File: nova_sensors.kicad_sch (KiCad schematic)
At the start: 91 parts, among them J1 Conn_01x03_Socket, J10 Conn_01x04_Socket, J11 Conn_01x04_Socket, J2 Conn_01x03_Socket, J3 Conn_01x04_Socket, J4 Conn_01x02_Socket, J5 Conn_01x02_Socket, J6 Conn_01x02_Socket, J7 Conn_01x02_Socket, J8 Conn_01x02_Socket, J9 Conn_01x02_Socket, SW1 SW_Push, SW2 SW_DIP_x02, SW3 SW_DIP_x02, U1 AT32F455CET7, U2 MAX3232, U3 MAX13487EESA+T, U4 MAX13487EESA+T, U5 LD1117S33TR, U6 XL1509-ADJ, Y1 8Mhz, Y2 32768hz

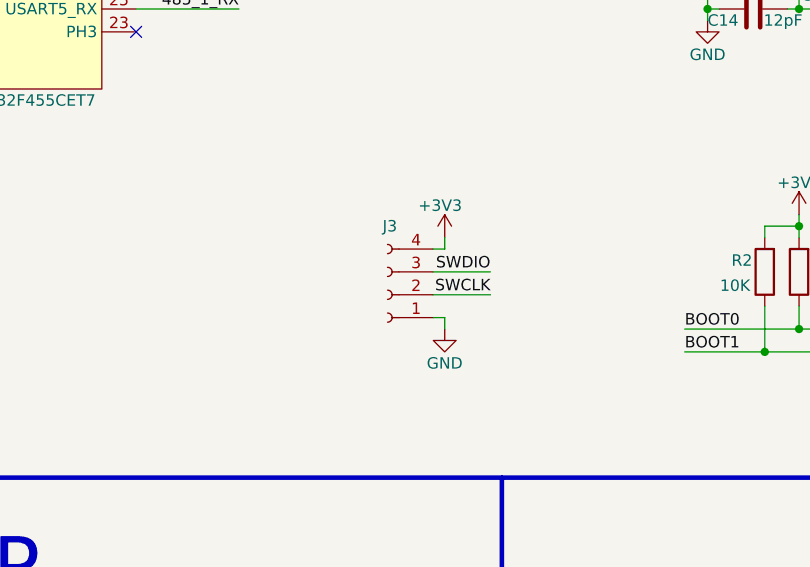
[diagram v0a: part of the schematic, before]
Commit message: fix: 修复debug口线序反了的问题
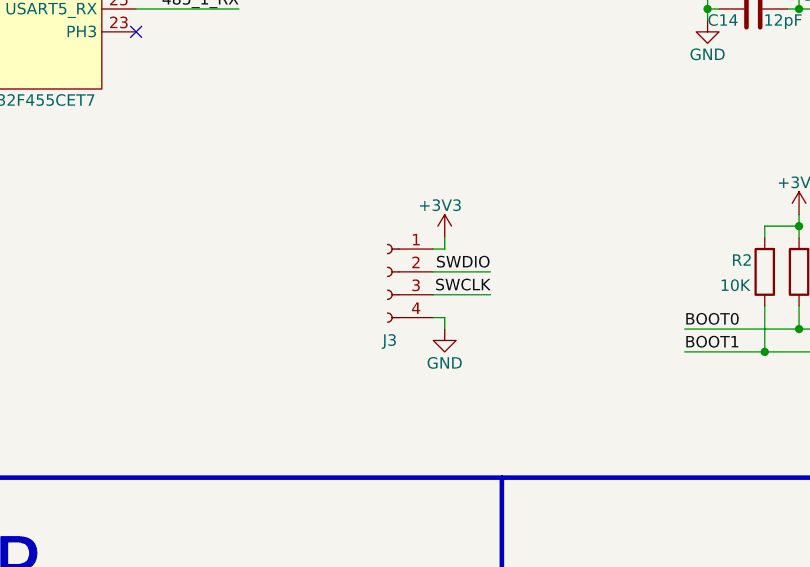
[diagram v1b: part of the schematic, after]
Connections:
- net +3V3: now also J3.1 (Pin_1); no longer J3.4 (Pin_4)
- net GND: now also J3.4 (Pin_4); no longer J3.1 (Pin_1)
- net SWCLK: now also J3.3 (Pin_3); no longer J3.2 (Pin_2)
- net SWDIO: now also J3.2 (Pin_2); no longer J3.3 (Pin_3)
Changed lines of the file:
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@@
-	)
-	(symbol
-		(lib_id "Connector:Conn_01x04_Socket")
-		(at 118.11 125.73 180)
-		(unit 1)
-		(body_style 1)
-		(exclude_from_sim no)
-		(in_bom yes)
-		(on_board yes)
-		(in_pos_files yes)
-		(dnp no)
-		(property "Reference" "J3"
-			(at 118.364 118.11 0)
-			(show_name no)
-			(do_not_autoplace no)
-			(effects
-				(font
-					(size 1.27 1.27)
-				)
-			)
-		)
-		(property "Value" "Conn_01x04_Socket"
-			(at 119.38 130.302 0)
-			(hide yes)
-			(show_name no)
-			(do_not_autoplace no)
-			(effects
-				(font
-					(size 1.27 1.27)
-				)
-			)
-		)
-		(property "Footprint" "Connector_JST:JST_XH_B4B-XH-A_1x04_P2.50mm_Vertical"
-			(at 118.11 125.73 0)
-			(hide yes)
-			(show_name no)
-			(do_not_autoplace no)
-			(effects
-				(font
-					(size 1.27 1.27)
-				)
-			)
-		)
-		(property "Datasheet" ""
-			(at 118.11 125.73 0)
-			(hide yes)
-			(show_name no)
-			(do_not_autoplace no)
-			(effects
-				(font
-					(size 1.27 1.27)
-				)
-			)
-		)
-		(property "Description" "Generic connector, single row, 01x04, script generated"
-			(at 118.11 125.73 0)
-			(hide yes)
-			(show_name no)
-			(do_not_autoplace no)
-			(effects
-				(font
-					(size 1.27 1.27)
-				)
-			)
-		)
-		(pin "1"
-		)
-		(pin "3"
-		)
-		(pin "2"
-		)
-		(pin "4"
-		)
-		(instances
-			(project "nova_sensors"
-				(path "/eb470288-4665-4cf2-a36a-110564d842a4"
-					(reference "J3")
-					(unit 1)
-				)
-			)
-		)
 	)
 	(symbol
@@
 					(unit 1)
 				)
+			)
+		)
+	)
+	(symbol
+		(lib_id "Connector:Conn_01x04_Socket")
+		(at 118.11 123.19 0)
+		(mirror y)
+		(unit 1)
+		(body_style 1)
+		(exclude_from_sim no)
+		(in_bom yes)
+		(on_board yes)
+		(in_pos_files yes)
+		(dnp no)
+		(property "Reference" "J3"
+			(at 118.364 130.81 0)
+			(show_name no)
+			(do_not_autoplace no)
+			(effects
+				(font
+					(size 1.27 1.27)
+				)
+			)
+		)
+		(property "Value" "Conn_01x04_Socket"
+			(at 119.38 118.618 0)
+			(hide yes)
+			(show_name no)
+			(do_not_autoplace no)
+			(effects
+				(font
+					(size 1.27 1.27)
+				)
+			)
+		)
+		(property "Footprint" "Connector_JST:JST_XH_B4B-XH-A_1x04_P2.50mm_Vertical"
+			(at 118.11 123.19 0)
+			(hide yes)
+			(show_name no)
+			(do_not_autoplace no)
+			(effects
+				(font
+					(size 1.27 1.27)
+				)
+			)
+		)
+		(property "Datasheet" ""
+			(at 118.11 123.19 0)
+			(hide yes)
+			(show_name no)
+			(do_not_autoplace no)
+			(effects
+				(font
+					(size 1.27 1.27)
+				)
+			)
+		)
+		(property "Description" "Generic connector, single row, 01x04, script generated"
+			(at 118.11 123.19 0)
+			(hide yes)
+			(show_name no)
+			(do_not_autoplace no)
+			(effects
+				(font
+					(size 1.27 1.27)
+				)
+			)
+		)
+		(pin "1"
+		)
+		(pin "3"
+		)
+		(pin "2"
+		)
+		(pin "4"
+		)
+		(instances
+			(project "nova_sensors"
+				(path "/eb470288-4665-4cf2-a36a-110564d842a4"
+					(reference "J3")
+					(unit 1)
+				)

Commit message: refact: 完成V0.0.2版本的布线和DRC检测
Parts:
- removed J6: Conn_01x02_Socket, Connector_Phoenix_MSTB:PhoenixContact_MSTBA_2,5_2-G-5,08_1x02_P5.08mm_Horizontal, symbol Connector:Conn_01x02_Socket
- added J6: Conn_01x03_Socket, Connector_Phoenix_MSTB:PhoenixContact_MSTBA_2,5_3-G-5,08_1x03_P5.08mm_Horizontal, symbol Connector:Conn_01x03_Socket
- added R19, R20: 4K7, Resistor_SMD:R_0603_1608Metric, symbol Device:R
- C25: value 22uF/16V -> 22uF/10V
- D1, D2, D3, D4: value SMAJ8.0CA -> SMAJ5.0CA
- U3, U4: value MAX13487EESA+T -> MAX13488EESA+T
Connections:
- net +3V3: now also R19.2, R20.2
- net GND: now also J6.3 (Pin_3)
- net TTL_RX: now also J6.2 (Pin_2), R20.1
- net TTL_TX: now also J6.1 (Pin_1), R19.1
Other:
- moved on the sheet: H1, H2, H3, H4

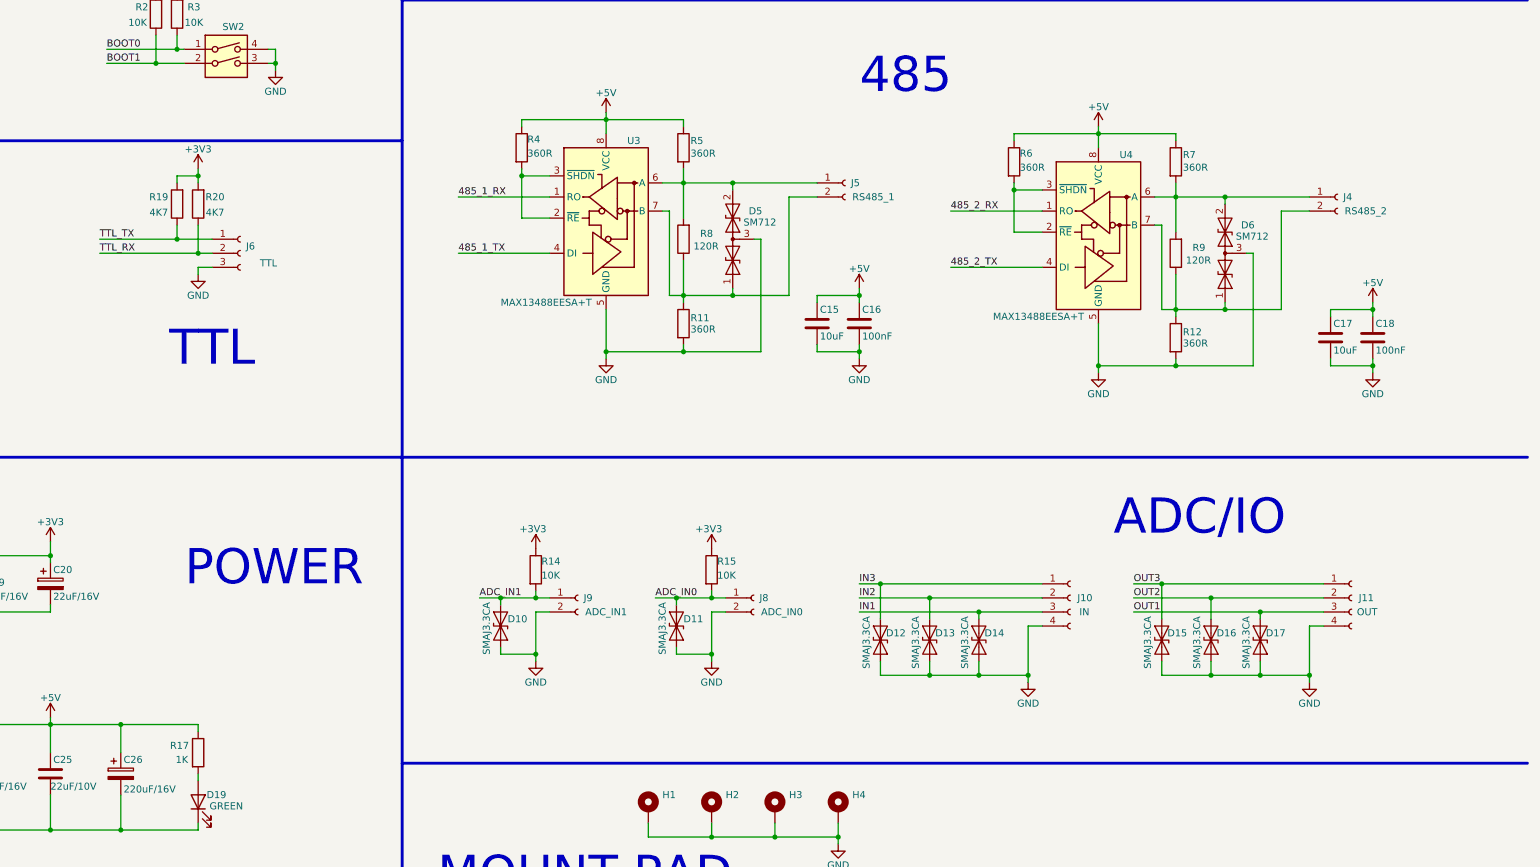
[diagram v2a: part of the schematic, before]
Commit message: refact: 调整PCB丝印和原理图符号位置
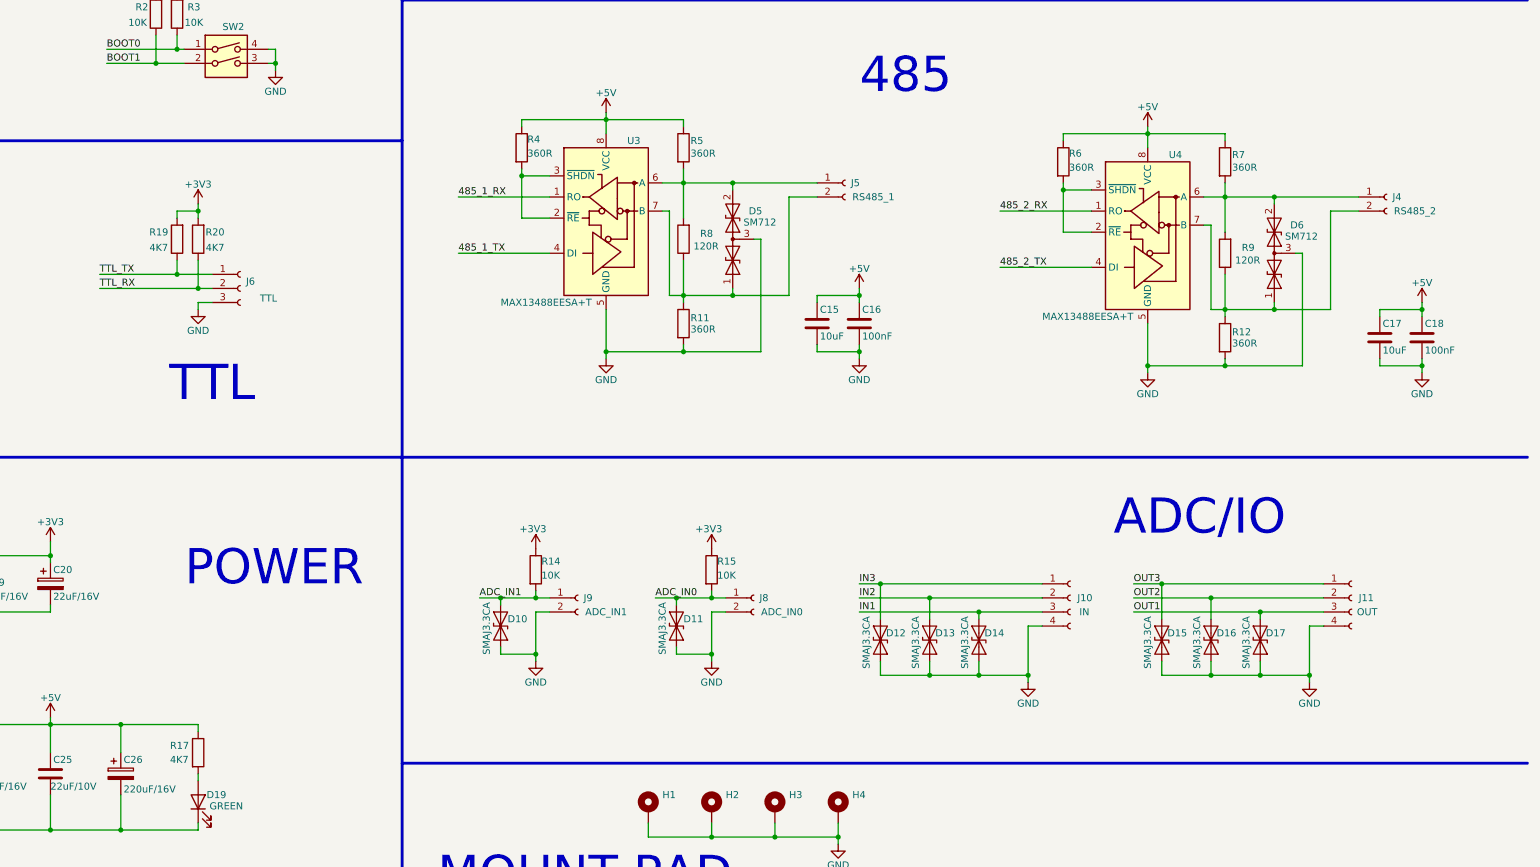
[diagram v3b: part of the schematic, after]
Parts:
- R17: value 1K -> 4K7
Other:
- moved on the sheet: C17, C18, D6, J4, J6, R12, R19, R20, R6, R7, R9, U4
